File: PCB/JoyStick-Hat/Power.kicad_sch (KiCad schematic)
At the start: 0 parts

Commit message: Power and LED Driver
Power Supply Schematic sketched out using Pololu power regulator modules to hasten design. LED drivers replaced with ones that have 24 ouputs so we can use 20 unit bar graph LEDs and have 8 extra channels for other onboard LEDs
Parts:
- added M1: D24V22F12, AVR-KiCAD-Lib-Modules:D24V22F12, symbol AVR-KiCAD-Lib-Modules:D24V22F12
- added M2: D24V22F5, AVR-KiCAD-Lib-Modules:D24V22F12, symbol AVR-KiCAD-Lib-Modules:D24V22F5
- added M3: D24V22F3, AVR-KiCAD-Lib-Modules:D24V22F12, symbol AVR-KiCAD-Lib-Modules:D24V22F3
- added R10, R2, R4: RC0603JR-07270RL, AVR-KiCAD-Lib-Resistors:R0603, symbol AVR-KiCAD-Lib-Resistors:RC0603JR-07270RL
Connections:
- new net +12V: M1.5 (VOUT)
- new net +24V: M1.3 (VIN), M2.3 (VIN), M3.3 (VIN)
- new net +3.3V: M3.5 (VOUT), R10.2, R2.2, R4.2
- new net +5V: M2.5 (VOUT)
- new net 12V_PG: M1.1 (PG), R2.1
- new net 3.3V_PG: M3.1 (PG), R10.1
- new net 5V_PG: M2.1 (PG), R4.1
- new net GND: M1.4 (GND), M2.4 (GND), M3.4 (GND)

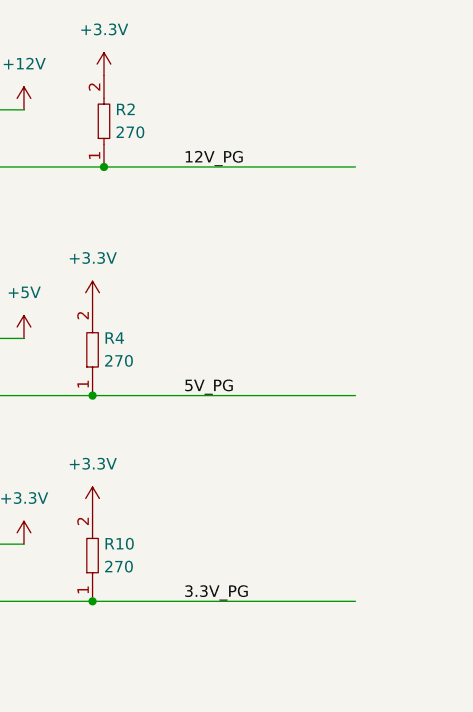
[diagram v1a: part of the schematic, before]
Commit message: Sheet Conenctivity and RS485
Added more sheet entries throughuot the project connecting different subsystems to the main MCU schematic. Also added  new sheet for the RS485 interface for communicating with the motor control board.
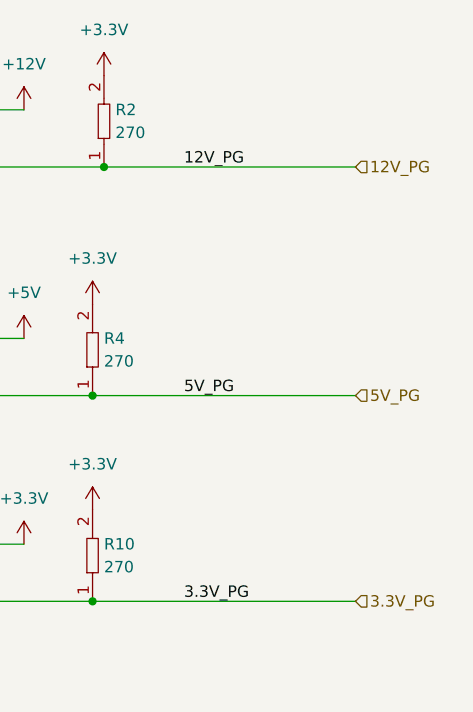
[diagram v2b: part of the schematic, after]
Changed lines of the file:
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@@
     (effects (font (size 1.27 1.27)) (justify left bottom))
+  )
+  (hierarchical_label "3.3V_PG" (shape input) (at 137.16 115.57 0) (fields_autoplaced)
+    (effects (font (size 1.27 1.27)) (justify left))
+  )
+  (hierarchical_label "5V_PG" (shape input) (at 137.16 92.71 0) (fields_autoplaced)
+    (effects (font (size 1.27 1.27)) (justify left))
+  )
+  (hierarchical_label "12V_PG" (shape input) (at 137.16 67.31 0) (fields_autoplaced)
+    (effects (font (size 1.27 1.27)) (justify left))
   )
   (symbol (lib_id "power:+3.3V") (at 107.95 105.41 0) (unit 1)

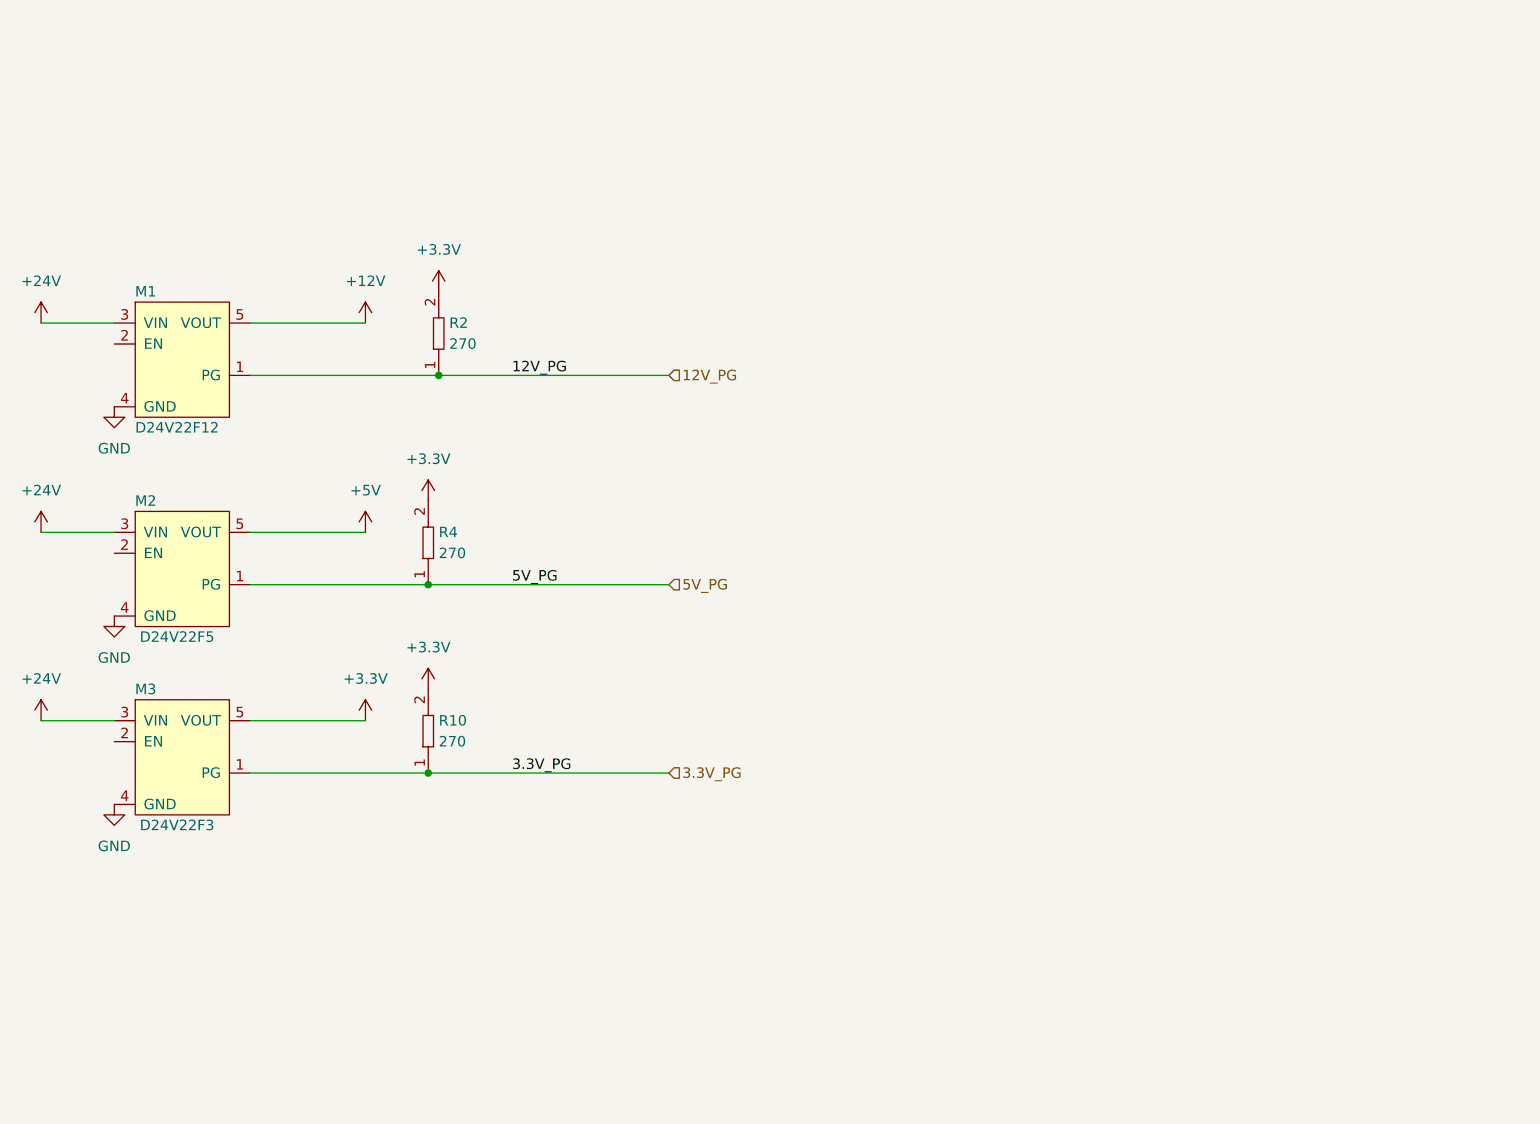
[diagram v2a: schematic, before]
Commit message: Schematic Progress
Made progress with schematic and corrected designator letters with connectors to match the built in paradigm of using J instead of T. T will not be used to referencing transformers instead of connectors.
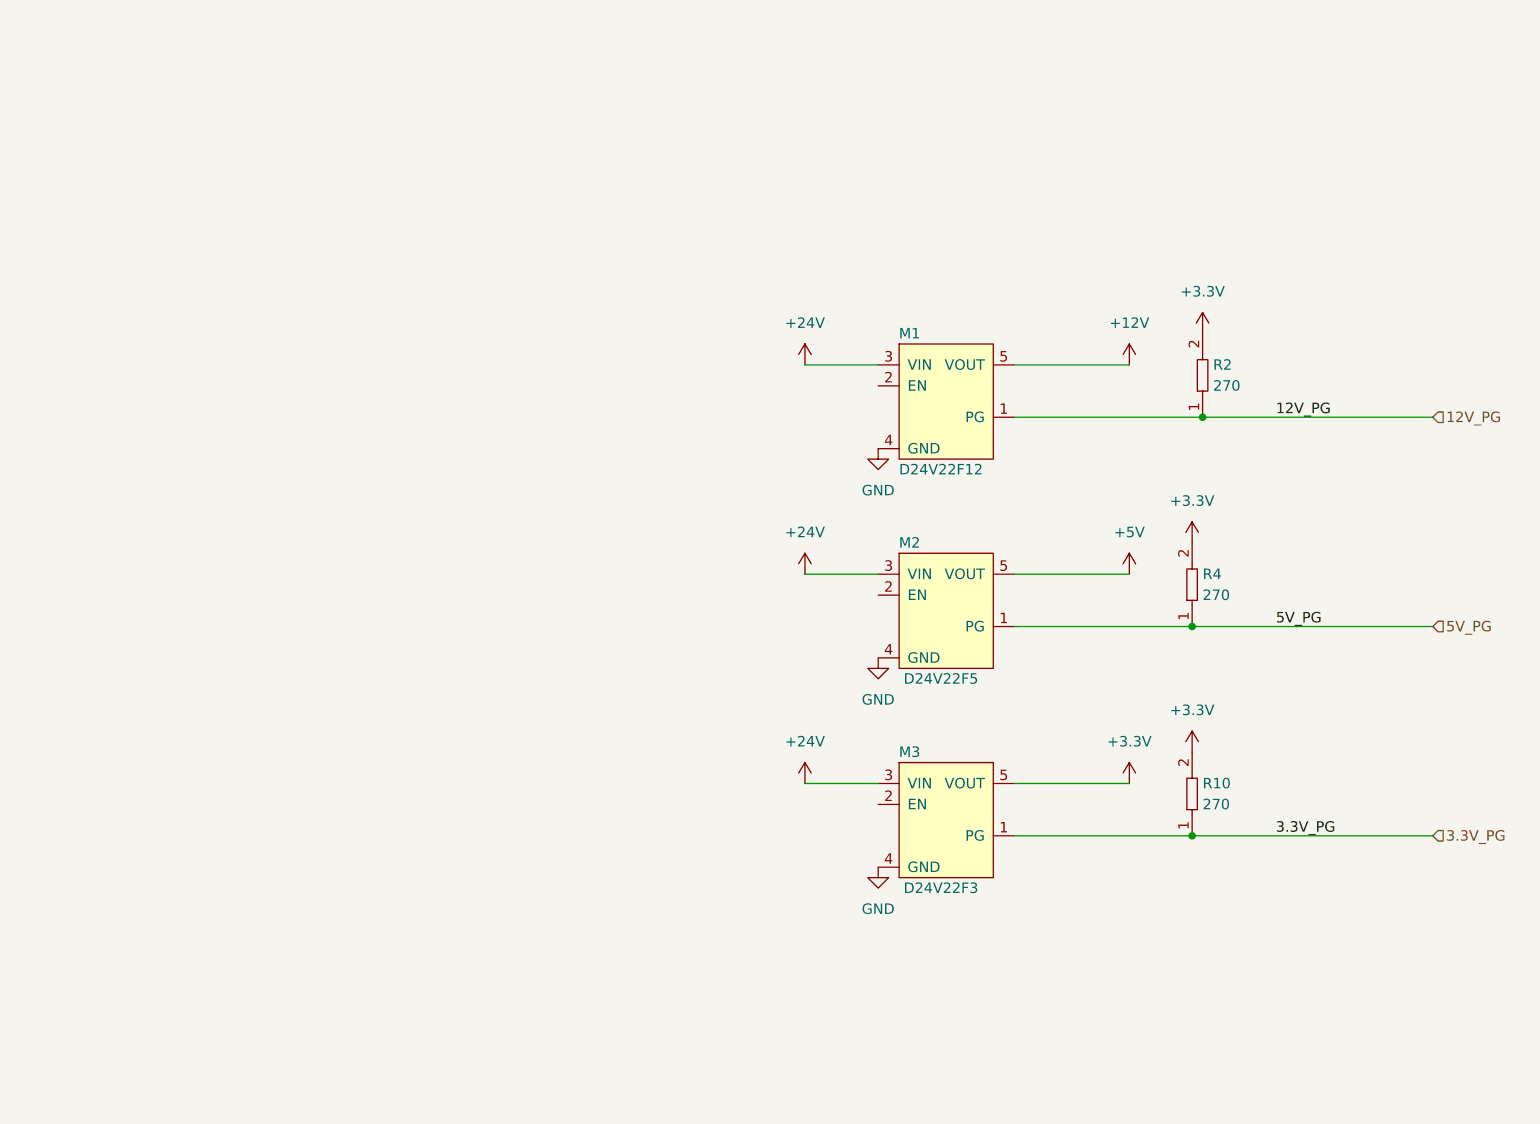
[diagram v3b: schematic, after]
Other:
- moved on the sheet: M1, M2, M3, R10, R2, R4

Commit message: LEDs and Additional connectors
Added heartbeat and diagnostic LEDs to STM32 and RPi3 schematics so we can directly flash them for debug purposes. Added a connector for serial port diagnostics on STM32. Added rotary switch interface for STM32 and added pullups to button connectors.
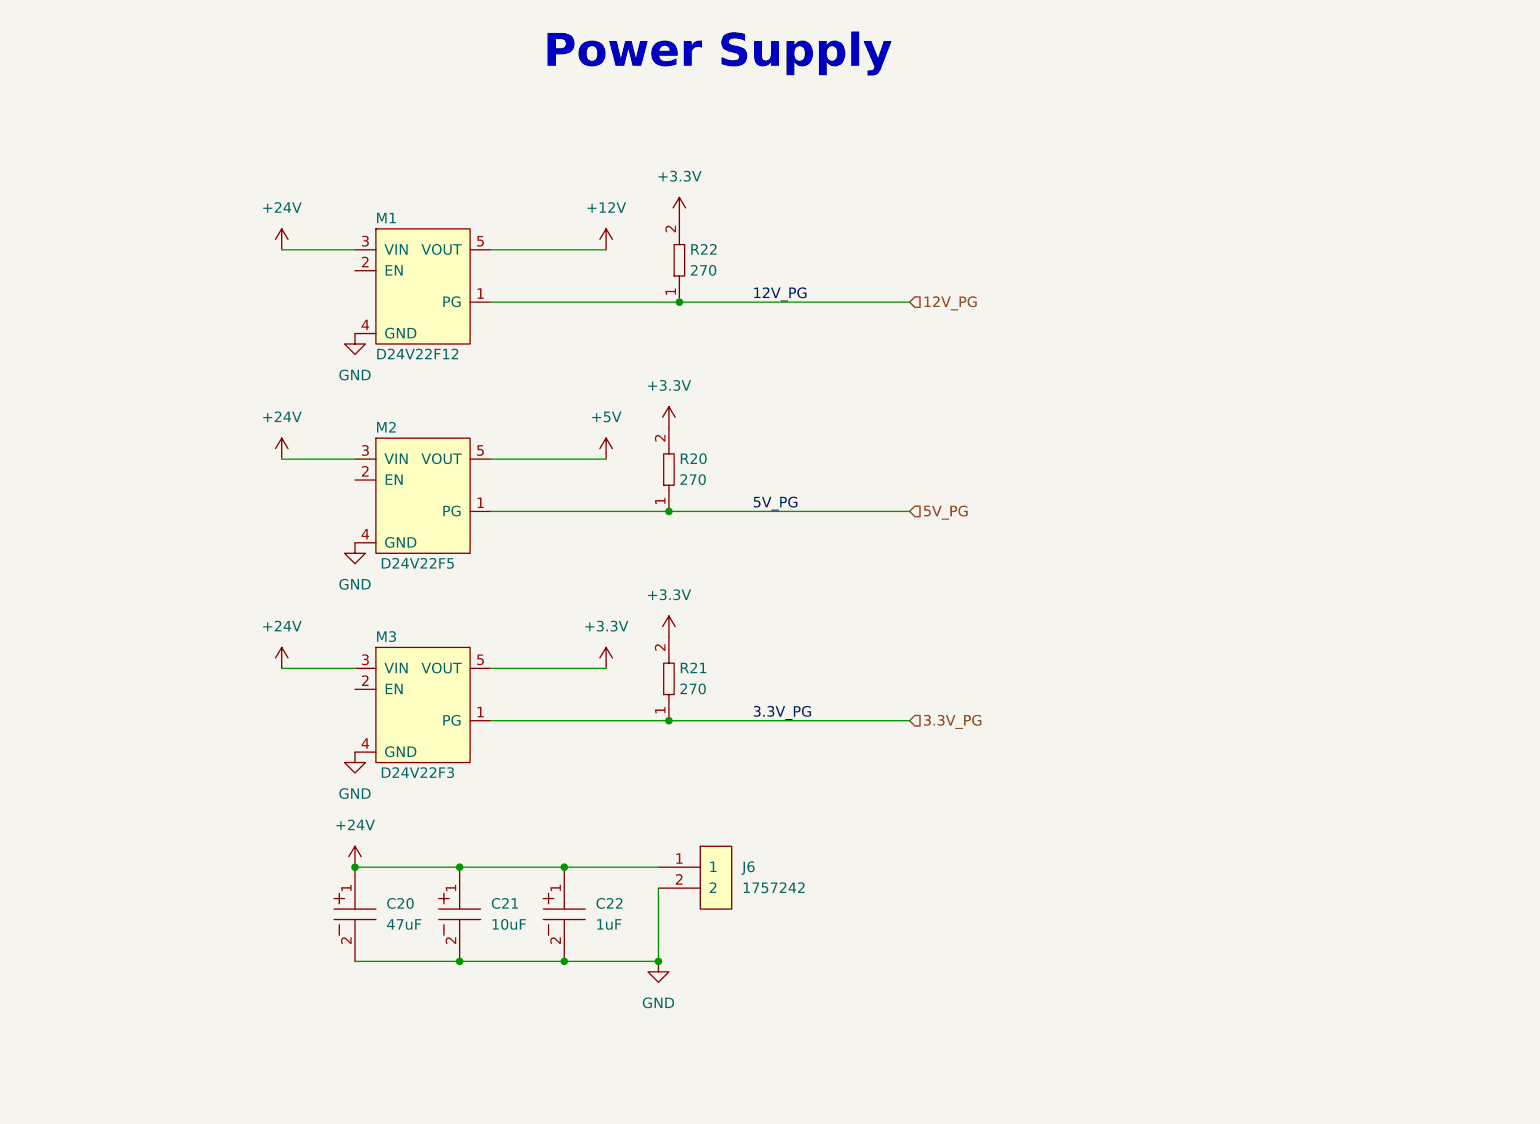
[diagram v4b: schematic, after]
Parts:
- added C20: UUQ1H470MCL1GS, AVR-KiCAD-Lib-Capacitors:CP_Elec_8x10, symbol AVR-KiCAD-Lib-Capacitors:UUQ1H470MCL1GS
- added C21: UUQ1H100MCL1GB, AVR-KiCAD-Lib-Capacitors:CP_Elec_4x5.3, symbol AVR-KiCAD-Lib-Capacitors:UUQ1H100MCL1GB
- added C22: UUQ1H010MCL1GB, AVR-KiCAD-Lib-Capacitors:CP_Elec_4x5.3, symbol AVR-KiCAD-Lib-Capacitors:UUQ1H010MCL1GB
- added J6: 1757242, AVR-KiCAD-Lib-Connectors:PhoenixContact_MSTBA-G_02x5.08mm_Angled, symbol AVR-KiCAD-Lib-Connectors:1757242
- renumbered R4 to R20, R10 to R21, R2 to R22
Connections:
- net +24V: now also C20.1, C21.1, C22.1, J6.1
- net GND: now also C20.2, C21.2, C22.2, J6.2
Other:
- note added: "Power Supply"
- moved on the sheet: M1, M2, M3, R20, R21, R22

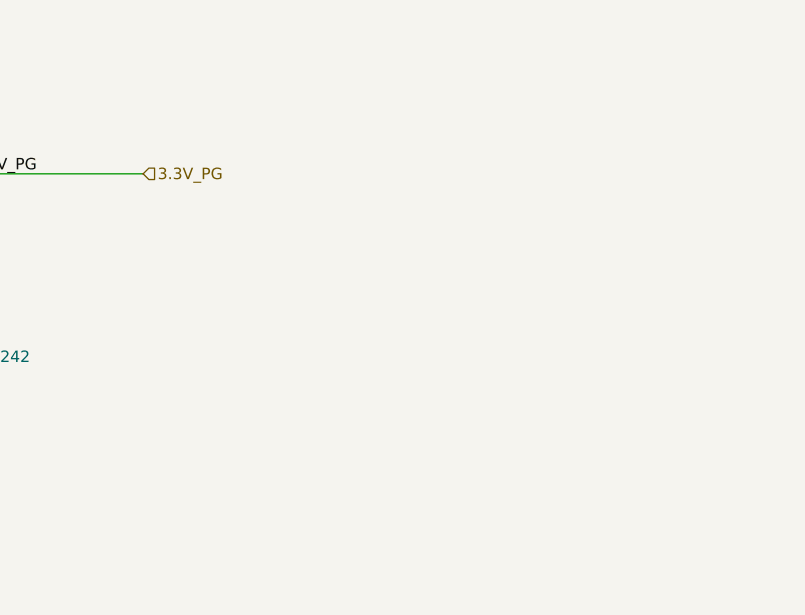
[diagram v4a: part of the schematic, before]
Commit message: Board Routing
Connectors swapped around and board route started
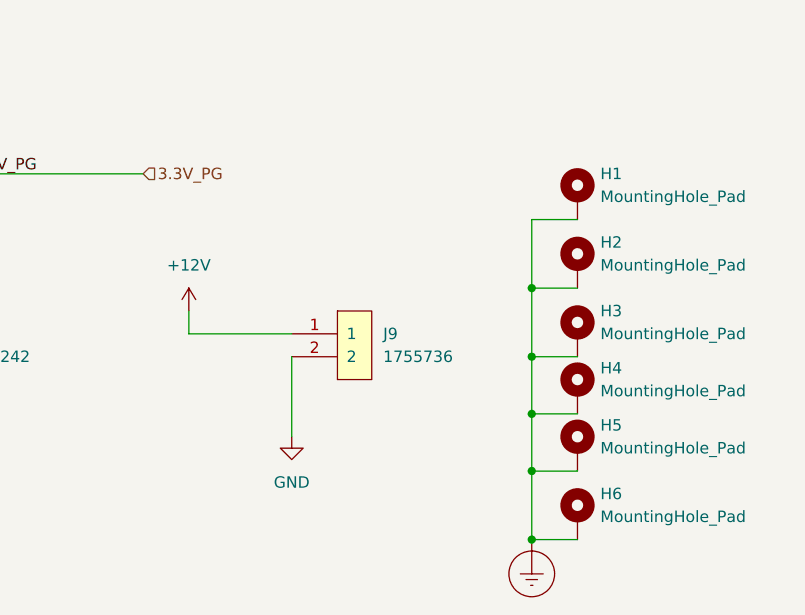
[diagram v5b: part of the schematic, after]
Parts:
- added H1, H2, H3, H4, H5, H6: MountingHole_Pad, AVR-KiCAD-Lib-Holes_Fasteners:RPI_HAT_HOLE, symbol Mechanical:MountingHole_Pad
- added J9: 1755736, AVR-KiCAD-Lib-Connectors:PhoenixContact_MSTBVA-G_02x5.08mm_Vertical, symbol AVR-KiCAD-Lib-Connectors:1755736
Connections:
- net +12V: now also J9.1
- net GND: now also J9.2
- new net Earth_Protective: H1.1, H2.1, H3.1, H4.1, H5.1, H6.1

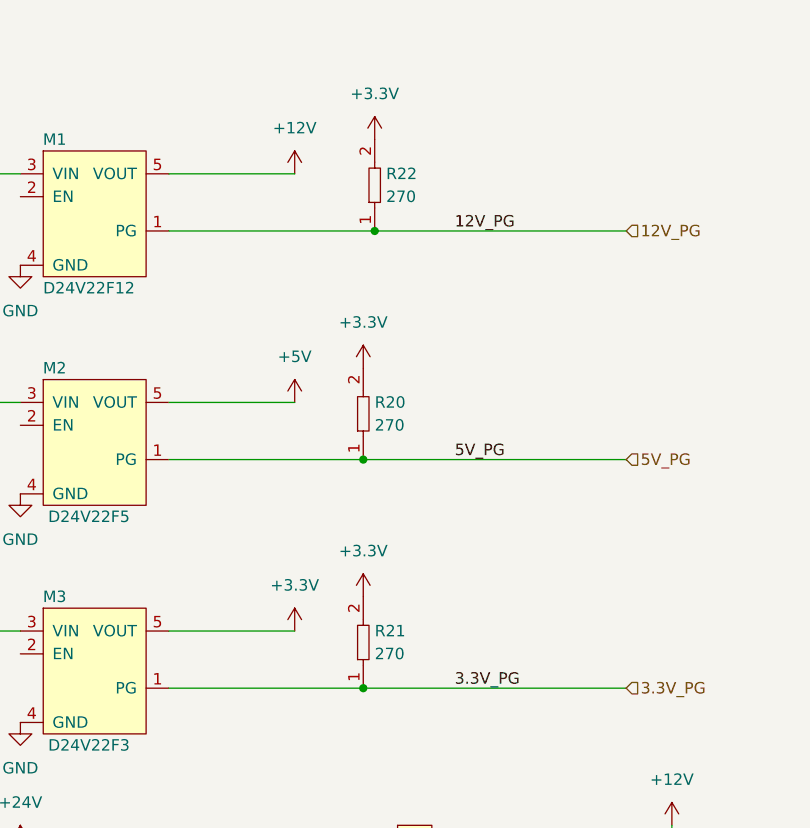
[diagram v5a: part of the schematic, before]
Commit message: James Fixes and 3D models
Added all the changes that James suggested to the design and then added 3D models to the board for mechanical design purposes. Generated 3D renders of the board and added them to new directory called img.
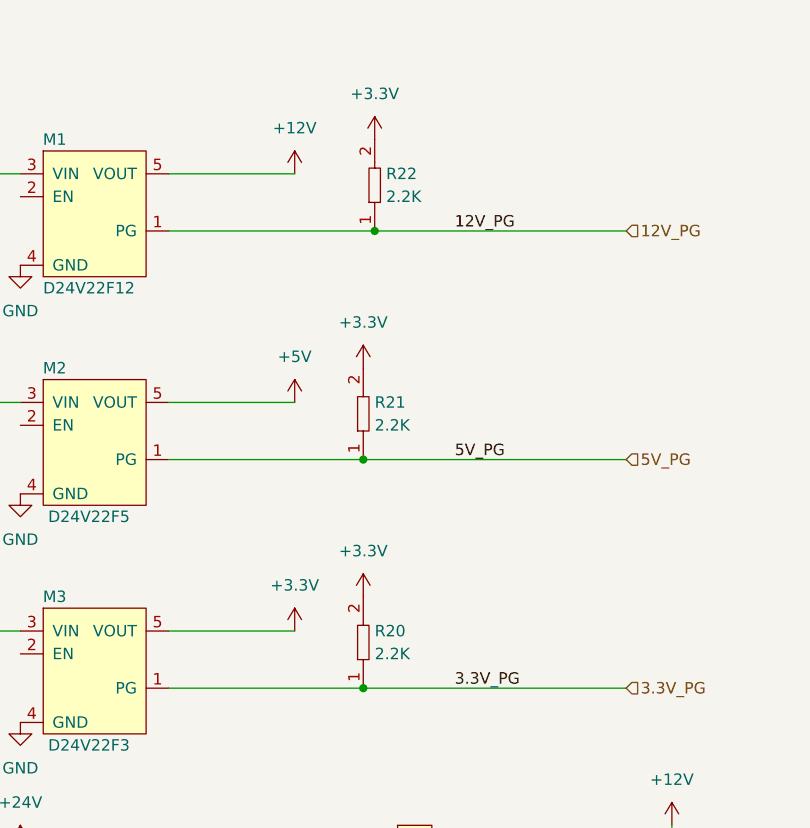
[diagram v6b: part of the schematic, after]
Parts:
- removed R20, R21, R22: RC0603JR-07270RL, AVR-KiCAD-Lib-Resistors:R0603, symbol AVR-KiCAD-Lib-Resistors:RC0603JR-07270RL
- added R20, R21, R22: RC0603FR-072K2L, AVR-KiCAD-Lib-Resistors:R0603, symbol AVR-KiCAD-Lib-Resistors:RC0603FR-072K2L
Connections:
- net +3.3V: now also R20.2, R21.2, R22.2
- net 12V_PG: now also R22.1
- net 3.3V_PG: now also R20.1
- net 5V_PG: now also R21.1
